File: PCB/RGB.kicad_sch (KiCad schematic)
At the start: 147 parts, among them J9 RGB_EX

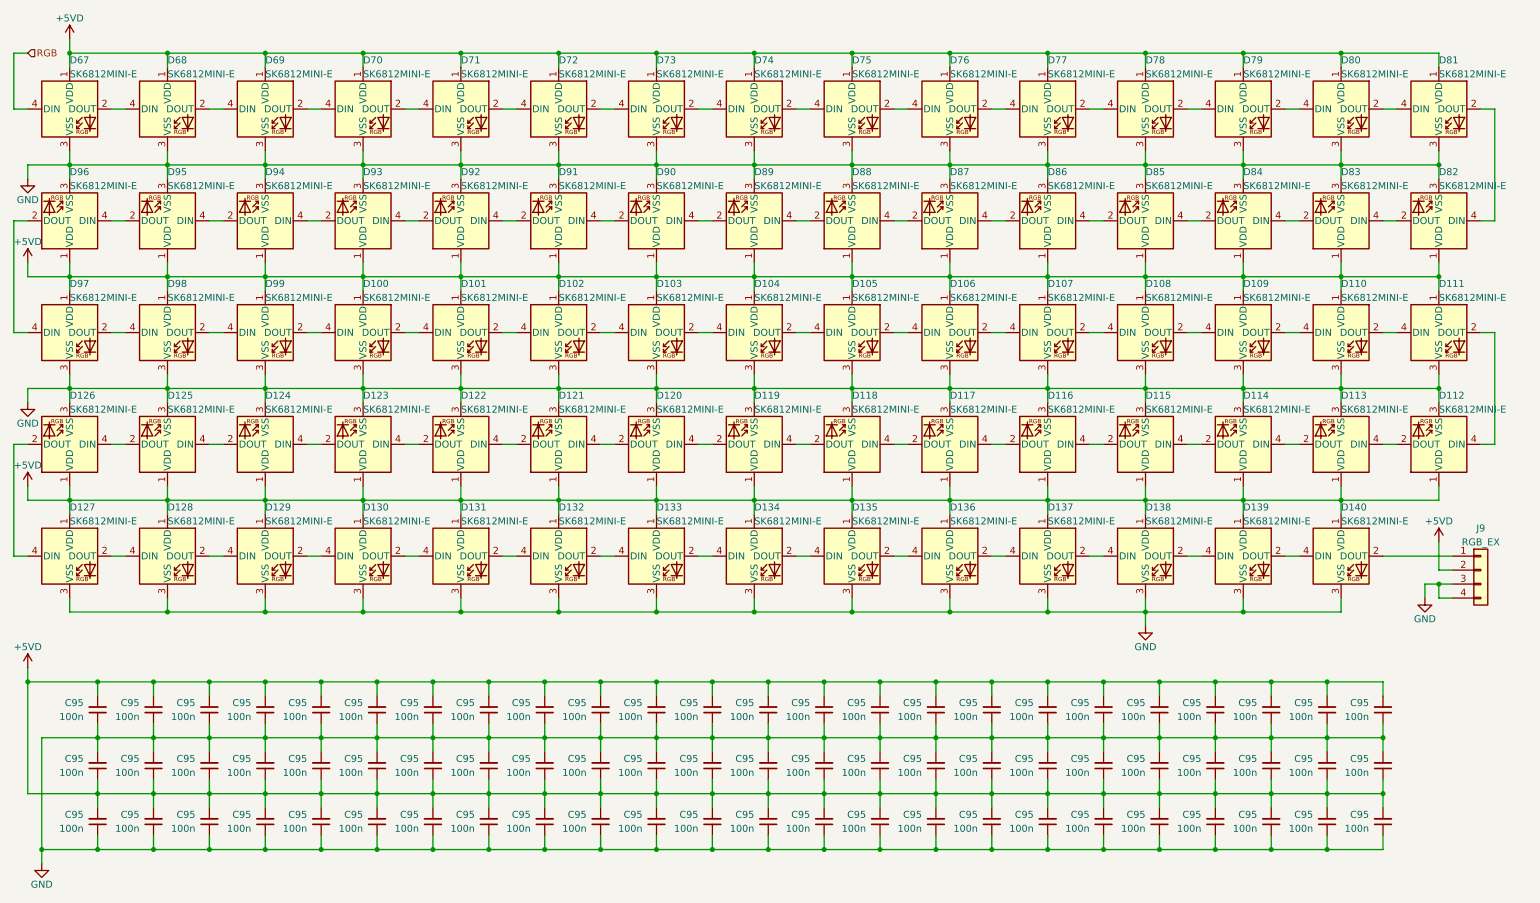
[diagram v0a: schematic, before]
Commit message: Finished routing RGB LEDs.
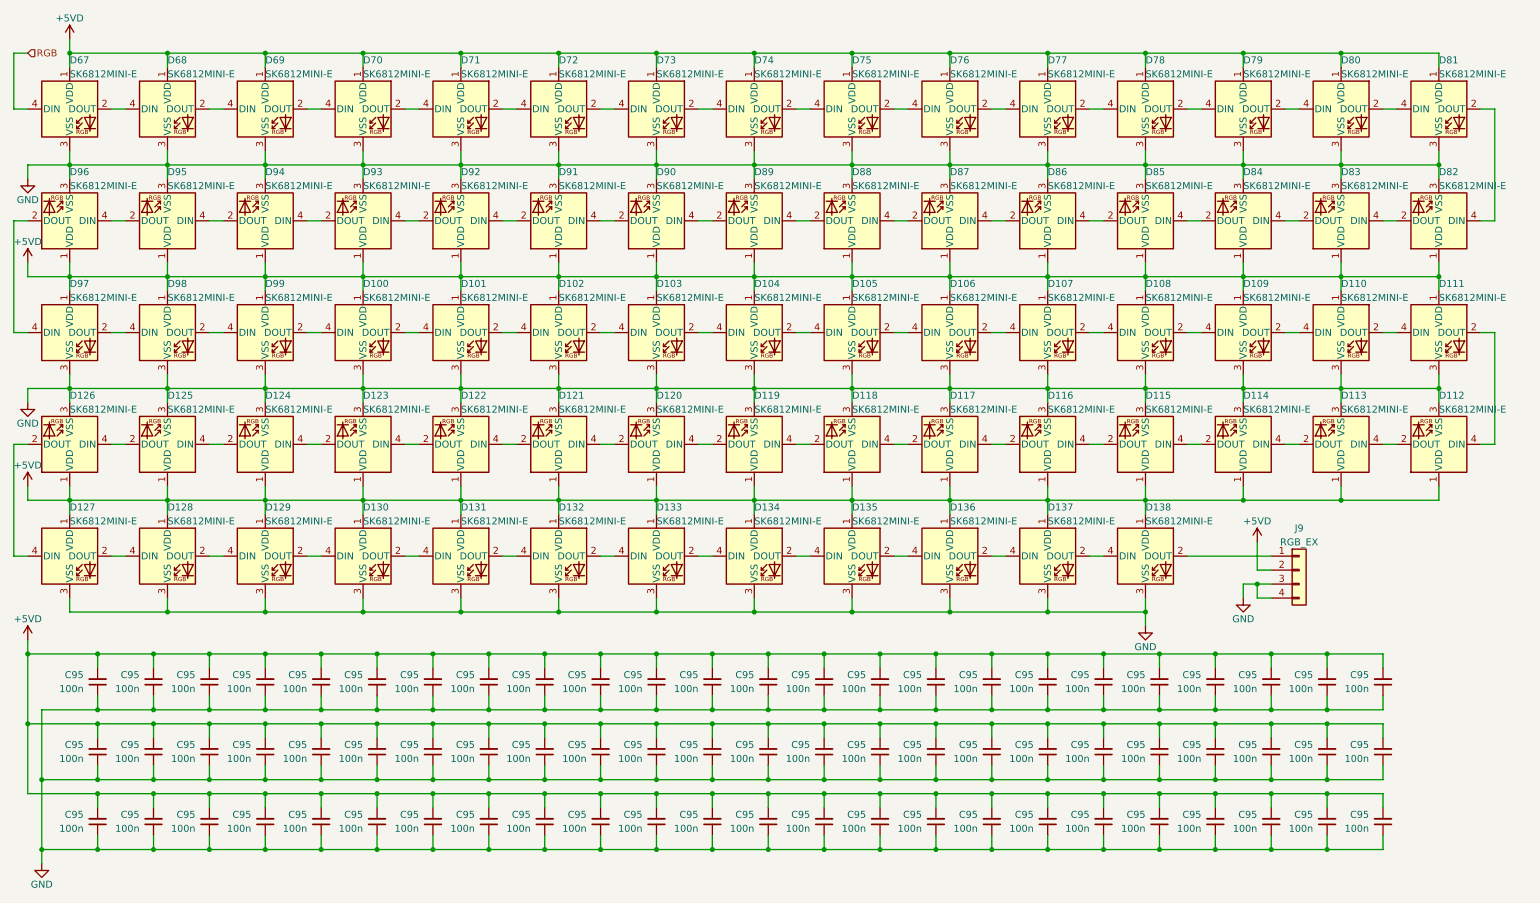
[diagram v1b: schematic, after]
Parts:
- removed C95 (x72): 100n, Capacitor_SMD:C_0402_1005Metric, symbol Device:C_Small
- removed D139, D140: SK6812MINI-E, Honeydew:YS-SK6812MINI-E, symbol Honeydew:SK6812MINI-E
- added C95 (x72): 100n, Honeydew:C_0402_1005Metric, symbol Device:C_Small
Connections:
- net +5VD: now also C95.2, C95.2, C95.2, C95.2, C95.2, C95.2, C95.2, C95.2, C95.2, C95.2, C95.2, C95.2, C95.2, C95.2, C95.2, C95.2, C95.2, C95.2, C95.2, C95.2, C95.2, C95.2, C95.2, C95.2, C95.2, C95.2, C95.2, C95.2, C95.2, C95.2, C95.2, C95.2, C95.2, C95.2, C95.2, C95.2, C95.2, C95.2, C95.2, C95.2, C95.2, C95.2, C95.2, C95.2, C95.2, C95.2, C95.2, C95.2, C95.2, C95.2, C95.2, C95.2, C95.2, C95.2, C95.2, C95.2, C95.2, C95.2, C95.2, C95.2, C95.2, C95.2, C95.2, C95.2, C95.2, C95.2, C95.2, C95.2, C95.2, C95.2, C95.2, C95.2
- net GND: now also C95.1, C95.1, C95.1, C95.1, C95.1, C95.1, C95.1, C95.1, C95.1, C95.1, C95.1, C95.1, C95.1, C95.1, C95.1, C95.1, C95.1, C95.1, C95.1, C95.1, C95.1, C95.1, C95.1, C95.1, C95.1, C95.1, C95.1, C95.1, C95.1, C95.1, C95.1, C95.1, C95.1, C95.1, C95.1, C95.1, C95.1, C95.1, C95.1, C95.1, C95.1, C95.1, C95.1, C95.1, C95.1, C95.1, C95.1, C95.1, C95.1, C95.1, C95.1, C95.1, C95.1, C95.1, C95.1, C95.1, C95.1, C95.1, C95.1, C95.1, C95.1, C95.1, C95.1, C95.1, C95.1, C95.1, C95.1, C95.1, C95.1, C95.1, C95.1, C95.1
- net at J9.1 (Pin_1): now also D138.2 (DOUT)
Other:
- moved on the sheet: J9

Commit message: Updated BOM. Added new tentative plate file.
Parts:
- D100, D101, D102, D103, D104, D105, D106, D107, D108, D109, D110, D111, D112, D113, D114, D115, D116, D117, D118, D119, D120, D121, D122, D123, D124, D125, D126, D127, D128, D129, D130, D131, D132, D133, D134, D135, D136, D137, D138, D67, D68, D69, D70, D71, D72, D73, D74, D75, D76, D77, D78, D79, D80, D81, D82, D83, D84, D85, D86, D87, D88, D89, D90, D91, D92, D93, D94, D95, D96, D97, D98, D99: LCSC C524051 -> C5242955

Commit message: In progress update
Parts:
- renumbered D67 to D1, D75 to D10, D74 to D11, D73 to D12, D79 to D13, D80 to D14, D81 to D15, D82 to D16, D83 to D17, D84 to D18, D90 to D19, D68 to D2, D89 to D20, D88 to D21, D87 to D22, D86 to D23, D85 to D24, D91 to D25, D92 to D26, D93 to D27, D94 to D28, D95 to D29, D69 to D3, D96 to D30, D130 to D31, D129 to D32, D128 to D33, D127 to D34, D126 to D35, D125 to D36, D119 to D37, D120 to D38, D121 to D39, D70 to D4, D122 to D40, D123 to D41, D124 to D42, D118 to D43, D117 to D44, D116 to D45, D115 to D46, D114 to D47, D113 to D48, D107 to D49, D71 to D5, D108 to D50, D109 to D51, D110 to D52, D111 to D53, D112 to D54, D106 to D55, D105 to D56, D104 to D57, D103 to D58, D102 to D59, D72 to D6, D101 to D60, D97 to D61, D98 to D62, D99 to D63, D100 to D64, D138 to D65, D137 to D66, D136 to D67, D135 to D68, D134 to D69, D78 to D7, D133 to D70, D132 to D71, D131 to D72, D77 to D8, D76 to D9
